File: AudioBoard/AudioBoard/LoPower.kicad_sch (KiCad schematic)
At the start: 0 parts

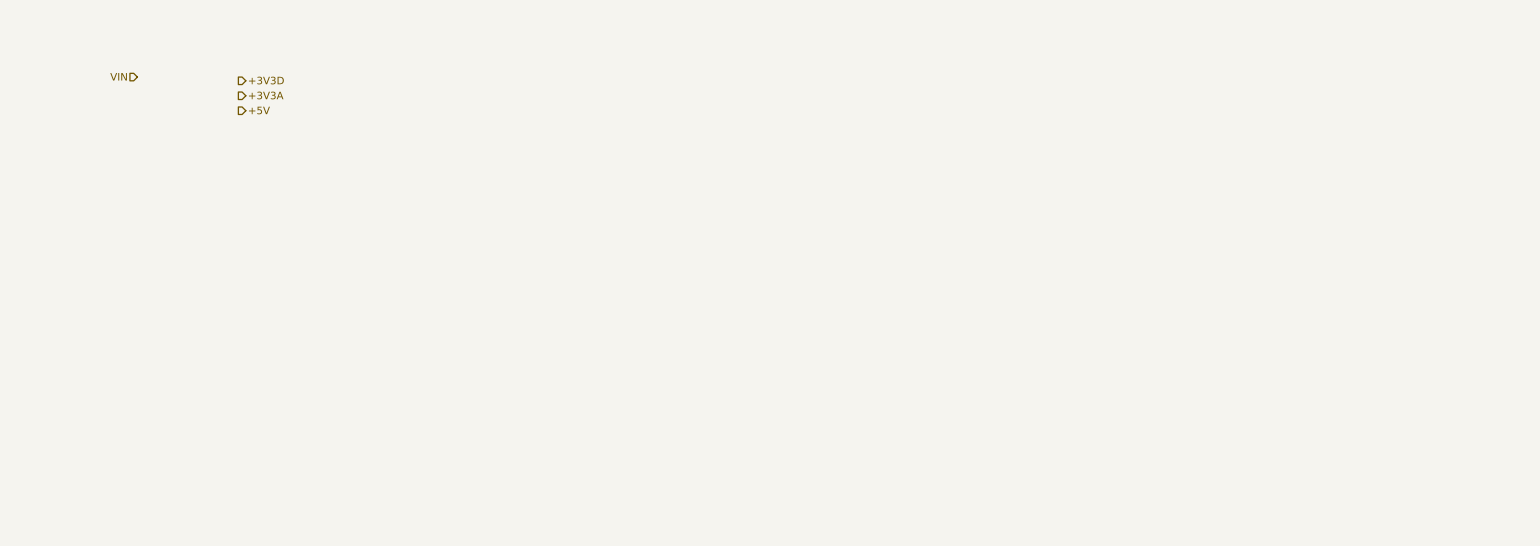
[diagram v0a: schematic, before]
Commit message: added power electronics
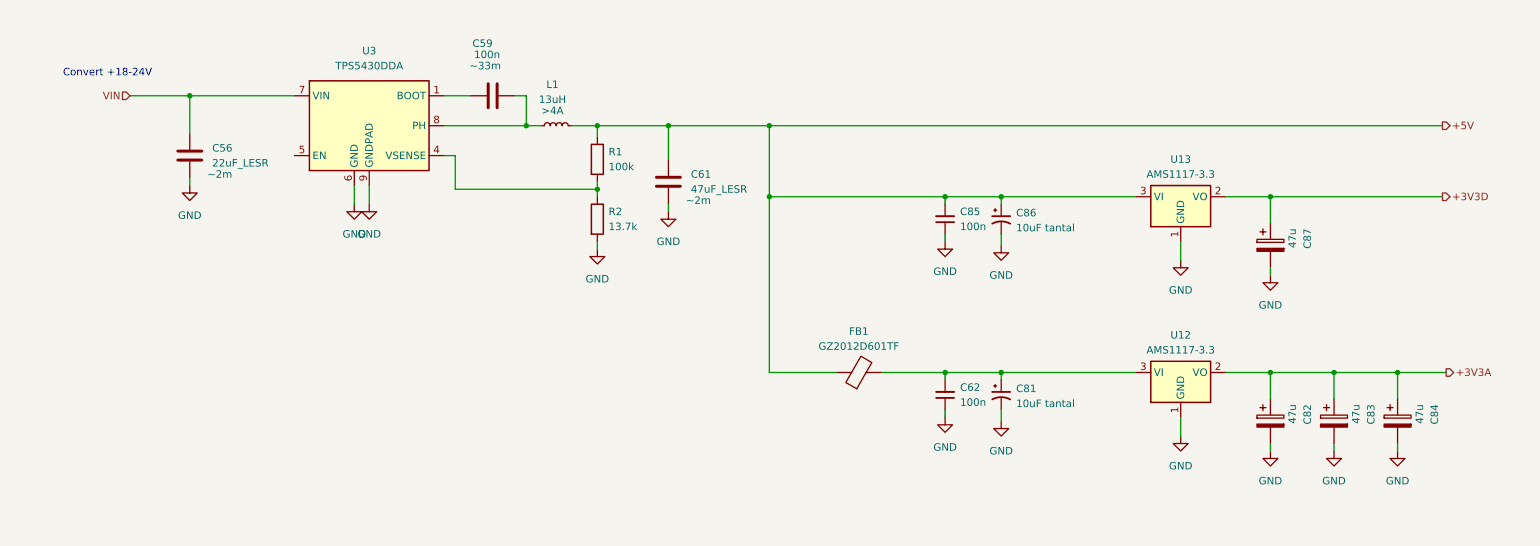
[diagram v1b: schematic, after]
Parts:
- added C56: 22uF_LESR, symbol Device:C
- added C59: 100n, symbol Device:C
- added C61: 47uF_LESR, symbol Device:C
- added C62, C85: 100n, Capacitor_SMD:C_0402_1005Metric, symbol Device:C_Small
- added C81, C86: 10uF tantal, Capacitor_Tantalum_SMD:CP_EIA-3216-18_Kemet-A, symbol Device:C_Polarized_Small_US
- added C82, C83, C84, C87: 47u, Capacitor_THT:CP_Radial_D6.3mm_P2.50mm, symbol Device:C_Polarized
- added FB1: GZ2012D601TF, Resistor_SMD:R_0805_2012Metric, symbol Device:FerriteBead
- added L1: 13uH, symbol Device:L_Small
- added R1: 100k, symbol Device:R
- added R2: 13.7k, symbol Device:R
- added U12, U13: AMS1117-3.3, Package_TO_SOT_SMD:SOT-223-3_TabPin2, symbol Regulator_Linear:AMS1117-3.3
- added U3: TPS5430DDA, Package_SO:TI_SO-PowerPAD-8_ThermalVias, symbol Regulator_Switching:TPS5430DDA
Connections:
- net +3V3A: now also C82.1, C83.1, C84.1, U12.2 (VO)
- net +3V3D: now also C87.1, U13.2 (VO)
- net +5V: now also C61.1, C85.2, C86.1, FB1.1, L1.2, R1.1, U13.3 (VI)
- net VIN: now also C56.1, U3.7 (VIN)
- new net: C62.2, C81.1, FB1.2, U12.3 (VI)
- new net: R1.2, R2.1, U3.4 (VSENSE)
- new net: C59.1, U3.1 (BOOT)
- new net: C59.2, L1.1, U3.8 (PH)
- new net GND: C56.2, C61.2, C62.1, C81.2, C82.2, C83.2, C84.2, C85.1, C86.2, C87.2, R2.2, U12.1 (GND), U13.1 (GND), U3.6 (GND), U3.9 (GNDPAD)
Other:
- note added: "Convert +18-24V"

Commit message: added power protection, dcdc modules
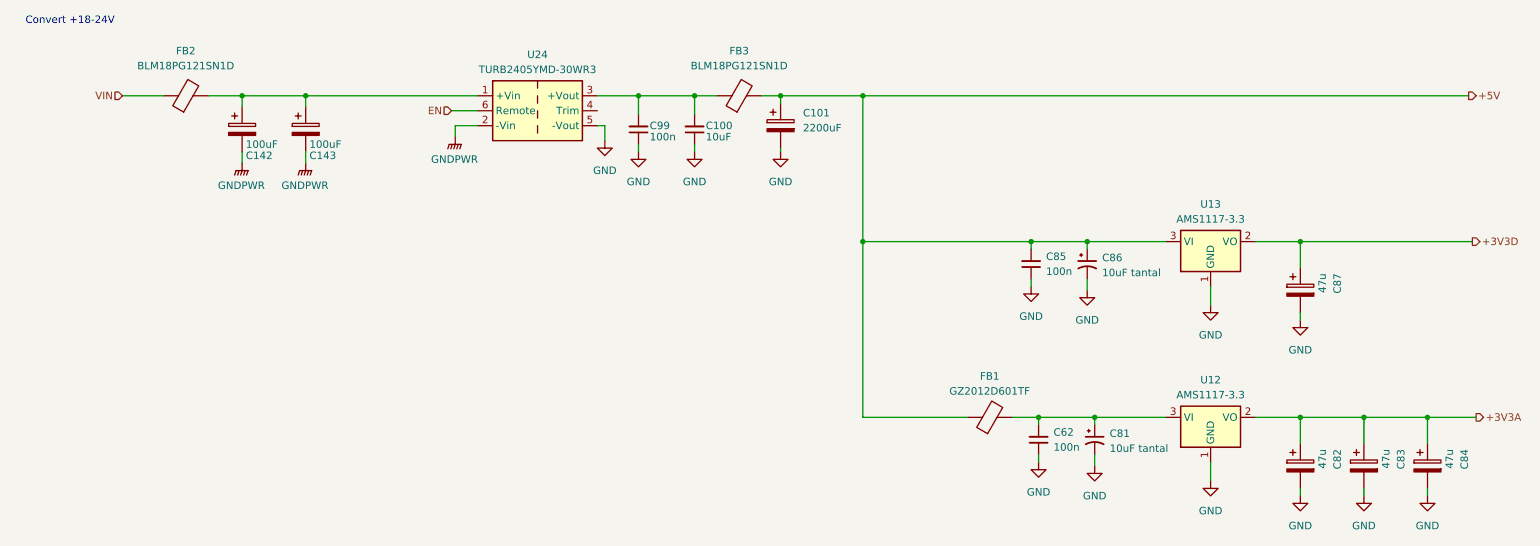
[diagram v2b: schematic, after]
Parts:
- removed C56: 22uF_LESR, symbol Device:C
- removed C59: 100n, symbol Device:C
- removed C61: 47uF_LESR, symbol Device:C
- removed L1: 13uH, symbol Device:L_Small
- removed R1: 100k, symbol Device:R
- removed R2: 13.7k, symbol Device:R
- removed U3: TPS5430DDA, Package_SO:TI_SO-PowerPAD-8_ThermalVias, symbol Regulator_Switching:TPS5430DDA
- added C100: 10uF, Capacitor_SMD:C_0402_1005Metric, symbol Device:C_Small
- added C101: 2200uF, Capacitor_THT:C_Radial_D16.0mm_H25.0mm_P7.50mm, symbol Device:C_Polarized
- added C142, C143: 100uF, symbol Device:C_Polarized
- added C99: 100n, Capacitor_SMD:C_0402_1005Metric, symbol Device:C_Small
- added FB2, FB3: BLM18PG121SN1D, Fuse:Fuse_0603_1608Metric, symbol Device:FerriteBead
- added U24: TURB2405YMD-30WR3, Converter_DCDC:Converter_DCDC_TRACO_THL30-xxxxWI_THT, symbol Converter_DCDC:THL30-4810WI
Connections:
- net +5V: now also C101.1, FB3.2
- net GND: now also C100.1, C101.2, C99.1, U24.5 (-Vout)
- net VIN: now also FB2.1
- new net: C100.2, C99.2, FB3.1, U24.3 (+Vout)
- new net: C142.1, C143.1, FB2.2, U24.1 (+Vin)
- new net EN: U24.6 (Remote)
- new net GNDPWR: C142.2, C143.2, U24.2 (-Vin)
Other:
- moved on the sheet: C62, C81, C82, C83, C84, C85, C86, C87, FB1, U12, U13

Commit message: assigned footprint to elements lcsc parts
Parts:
- C101: JLCPCB (none) -> C105334; LCSC Part (none) -> C105334
- C142, C143: footprint (none) -> Capacitor_SMD:CP_Elec_5x5.4; JLCPCB (none) -> C48970701; LCSC Part (none) -> C48970701
- FB2, FB3: JLCPCB (none) -> C14709; LCSC Part (none) -> C14709; lcsc part C14709 -> (none)
- U12, U13: JLCPCB (none) -> C6186; LCSC Part (none) -> C6186
